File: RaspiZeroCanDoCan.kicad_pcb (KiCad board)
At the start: 2 copper layers, 14 parts, among them P1 CAN_conn, P2 CAN_conn, U1 MCP2515-E/ST, U2 MCP2562-E/SN

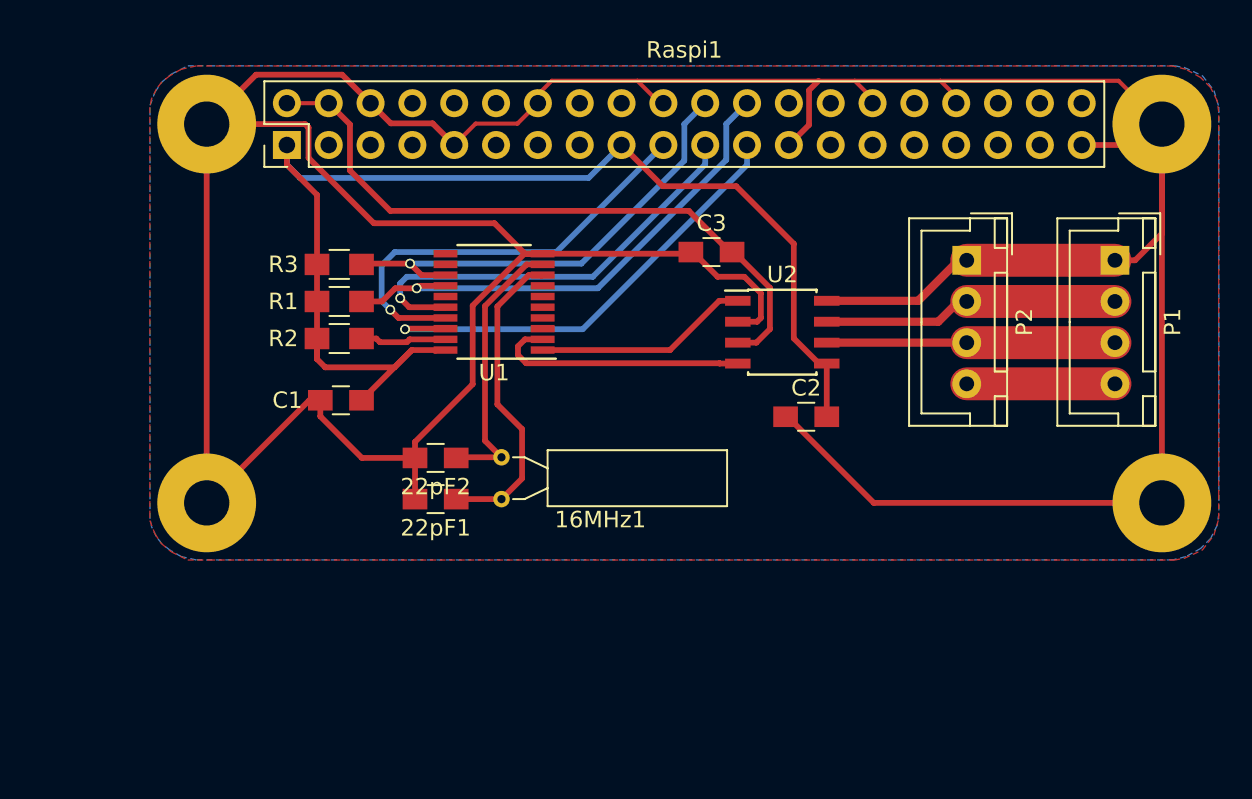
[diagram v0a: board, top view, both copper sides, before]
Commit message: Back from scratch design with power from bus
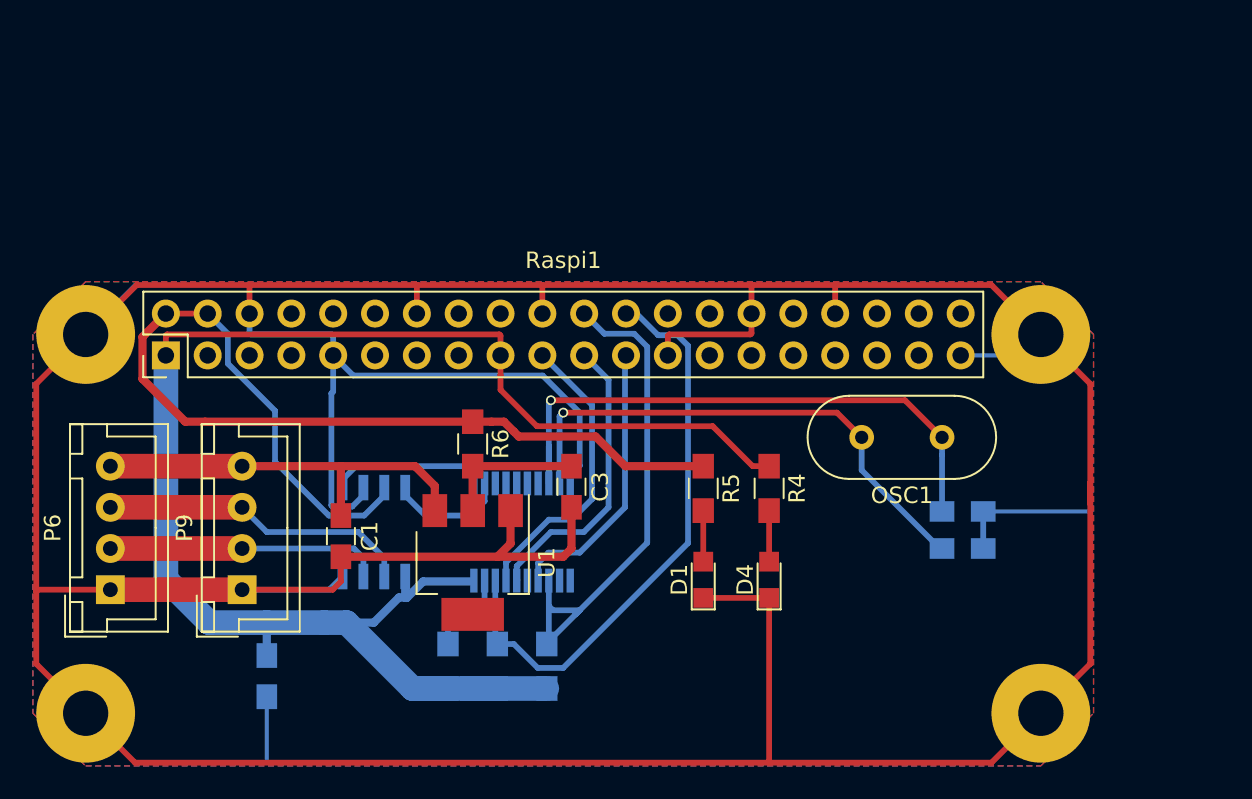
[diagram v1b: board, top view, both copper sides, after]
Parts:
- removed 16MHz1: Crystal, Crystals:Crystal_AT310_d3.0mm_l10.0mm_Horizontal
- removed 22pF1, 22pF2: C, Capacitors_SMD:C_0805_HandSoldering
- removed P1, P2: CAN_conn, Connectors_JST:JST_XH_B04B-XH-A_04x2.50mm_Straight
- removed U2: MCP2562-E/SN, Housings_SOIC:SOIC-8_3.9x4.9mm_Pitch1.27mm
- added C4: 22pF, Capacitors_SMD:C_0805_HandSoldering, B.Cu at (172.8, 118.0)
- added C5: C, Capacitors_SMD:C_0805_HandSoldering, B.Cu at (130.5, 125.8)
- added D1: LED PWR, LEDs:LED_0805, F.Cu at (157.0, 119.9)
- added D4: LED PWR, LEDs:LED_0805, F.Cu at (161.0, 119.9)
- added IC1: MCP2562, Housings_SOIC:SOIC-8_3.9x4.9mm_Pitch1.27mm, B.Cu at (137.0, 117.0)
- added OSC1: 16MHz, Crystals:Crystal_HC49-4H_Vertical, F.Cu at (171.5, 111.2)
- added P6: CAN_conn, Connectors_JST:JST_XH_B04B-XH-A_04x2.50mm_Straight, F.Cu at (121.0, 120.5)
- added P9: CAN_conn, Connectors_JST:JST_XH_B04B-XH-A_04x2.50mm_Straight, F.Cu at (129.0, 120.5)
- added R4: R, Resistors_SMD:R_0805_HandSoldering, F.Cu at (161.0, 114.3)
- added R5: R, Resistors_SMD:R_0805_HandSoldering, F.Cu at (157.0, 114.3)
- added R6: 0, Resistors_SMD:R_0805_HandSoldering, F.Cu at (143.0, 111.7)
- added U3: MCP2515-E/ST, Housings_SSOP:TSSOP-20_4.4x6.5mm_Pitch0.65mm, B.Cu at (146.0, 117.0)
- C1: value C_Small -> 100nF
- C2: value C_Small -> 22pF; moved to B.Cu
- C3: value C_Small -> 10uF
- R1, R2, R3: moved to B.Cu
- Raspi1: value RaspiZeroCanDoCan -> Raspberry_Pi_2_3
- U1: value MCP2515-E/ST -> LD1117S50TR; footprint Housings_SSOP:TSSOP-20_4.4x6.5mm_Pitch0.65mm -> TO_SOT_Packages_SMD:SOT-223
- moved R3 27.5 mm to (147.5, 125.2), turned to 90 degrees
- moved R1 24.1 mm to (144.5, 125.2), turned to 270 degrees
- moved R2 21.0 mm to (141.5, 125.2), turned to 90 degrees
- moved C3 16.6 mm to (149.0, 114.2), turned to 270 degrees
- moved U1 15.9 mm to (143.0, 118.8), turned to 270 degrees
- moved Raspi1 14.7 mm to (148.5, 105.0)
- moved C2 11.1 mm to (172.8, 115.8)
- moved C1 8.25 mm to (135.0, 117.2), turned to 270 degrees
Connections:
- C1 pad 1: GND -> +9V
- C1 pad 2: +3V3 -> GND
- C2 pad 1: GND -> Net-(C2-Pad1)
- C2 pad 2: +3V3 -> GND
- C3 pad 1: GND -> Net-(C3-Pad1)
- C3 pad 2: +5V -> GND
- U1 pad 1: Net-(U1-Pad1) -> GND
- U1 pad 2: Net-(U1-Pad2) -> Net-(C3-Pad1)
- U1 pad 3: Net-(U1-Pad3) -> +9V
- U1 pad 4: Net-(U1-Pad4) -> (no net)
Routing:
- net GND: track 257.5 -> 489.3 mm
- net Net-(C2-Pad1): track 0.00 -> 36.6 mm, vias 0 -> 1
- net Net-(C4-Pad1): track 0.00 -> 32.0 mm, vias 0 -> 1
- net +3V3: track 75.3 -> 106.1 mm
- net +9V: track 0.00 -> 24.7 mm
- net +5V: track 40.4 -> 63.0 mm
- net Net-(16MHz1-Pad1): track 19.2 -> 0.00 mm
- net Net-(16MHz1-Pad2): track 16.9 -> 0.00 mm
- net Net-(U1-Pad2): track 15.8 -> 0.00 mm
- net Net-(U1-Pad1): track 13.1 -> 0.00 mm
- net SPI_CLK: track 29.2 -> 17.0 mm, vias 1 -> 0
- net CAN_TX: track 0.00 -> 9.80 mm
- net CAN_POW: track 9.00 -> 0.00 mm
- net SPI_MISO: track 26.6 -> 17.8 mm, vias 1 -> 0
- net SPI_MOSI: track 26.6 -> 17.9 mm, vias 1 -> 0
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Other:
- net class DRC added: clearance 0.65, trace_width 0.5, via_dia 0.6, via_drill 0.4
- net class Default: trace_width 0.35 -> 0.25
- net class Interm added: clearance 0.4, trace_width 0.5, via_dia 0.6, via_drill 0.4
- net class POPOW removed
- net class PWR added: clearance 0.8, trace_width 1.5, via_dia 0.6, via_drill 0.4
- net class Power removed
- net class Signal added: clearance 0.2, trace_width 0.25, via_dia 0.6, via_drill 0.4

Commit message: removed a capa, cleaned top layer
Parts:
- added C6: C, Capacitors_SMD:C_0805_HandSoldering, B.Cu at (132.5, 110.5)
- moved D1 10.3 mm to (148.0, 124.9)
- moved D4 10.3 mm to (152.0, 124.9)
- moved R4 10.3 mm to (152.0, 119.3)
- moved R5 10.3 mm to (148.0, 119.3)
- moved C3 7.04 mm to (142.0, 113.5), turned to 0 degrees
- moved R6 5.77 mm to (137.3, 110.5), turned to 0 degrees
- moved U1 2.34 mm to (140.8, 119.7)
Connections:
- C3 pad 1: Net-(C3-Pad1) -> CAN_5V
- R5 pad 1: +5V -> CAN_5V
- R6 pad 2: Net-(C3-Pad1) -> CAN_5V
- U1 pad 2: Net-(C3-Pad1) -> CAN_5V
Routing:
- net +5V: track 63.0 -> 42.1 mm
- net CAN_5V: track 0.00 -> 19.4 mm
- net Net-(C3-Pad1): track 8.70 -> 0.00 mm
- net +3V3: track 106.1 -> 99.2 mm
- net GND: track 489.3 -> 485.4 mm
- net Net-(C2-Pad1): track 36.6 -> 34.3 mm
- net +9V: track 24.7 -> 24.1 mm

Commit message: pcb refactoring
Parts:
- R1, R2, R3, U3: moved to F.Cu
- moved D1 22.8 mm to (170.0, 118.9)
- moved D4 22.8 mm to (174.0, 118.9)
- moved R4 22.8 mm to (174.0, 113.3)
- moved R5 22.8 mm to (170.0, 113.3)
- moved R3 17.1 mm to (155.5, 110.0), turned to 180 degrees
- moved R1 15.2 mm to (146.0, 110.0), turned to 180 degrees
- moved OSC1 13.1 mm to (160.0, 117.6), turned to 270 degrees
- moved R2 10.9 mm to (146.5, 115.5)
- moved C2 8.75 mm to (165.2, 120.2)
- moved C4 8.75 mm to (165.2, 122.5)
- moved U3 6.41 mm to (151.9, 119.5), turned to 90 degrees
- moved C5 3.54 mm to (134.0, 125.2)
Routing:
- net Net-(C4-Pad1): track 32.0 -> 11.6 mm, vias 1 -> 0
- net Net-(C2-Pad1): track 34.3 -> 14.2 mm, vias 1 -> 0
- net CAN_5V: track 19.4 -> 37.4 mm, vias 0 -> 2
- net SPI_CS0: track 35.8 -> 19.7 mm
- net GND: track 485.4 -> 471.0 mm
- net INT: track 31.5 -> 18.4 mm
- net CAN_RX: track 7.24 -> 17.4 mm, vias 0 -> 1
- net CAN_TX: track 9.80 -> 19.4 mm, vias 0 -> 1
- net +3V3: track 99.2 -> 108.8 mm
- net SPI_MISO: track 17.8 -> 11.0 mm
- net SPI_CLK: track 17.0 -> 10.5 mm
- net SPI_MOSI: track 17.9 -> 11.8 mm
- net Net-(R2-Pad2): track 5.36 -> 4.75 mm
